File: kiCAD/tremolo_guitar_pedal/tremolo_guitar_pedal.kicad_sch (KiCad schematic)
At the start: 47 parts, among them J1 1/4" Mono Jack, J2 1/4" Mono Jack, J4 Barrel_Jack, J5 UPduino v3.1, SW1 3PDT Footswitch, SW2 3PDT Footswitch, SW3 3PDT Footswitch, SW4 SW_Depth, SW5 SW_Speed, U1 MCP6002-xP, U2 MCP6002-xP, U3 LD1117DT33CTR, U3 MCP6002-xP, U4 NUCLEO-LxxxKx, U5 PCM5102, U7 UPduino_v3.1

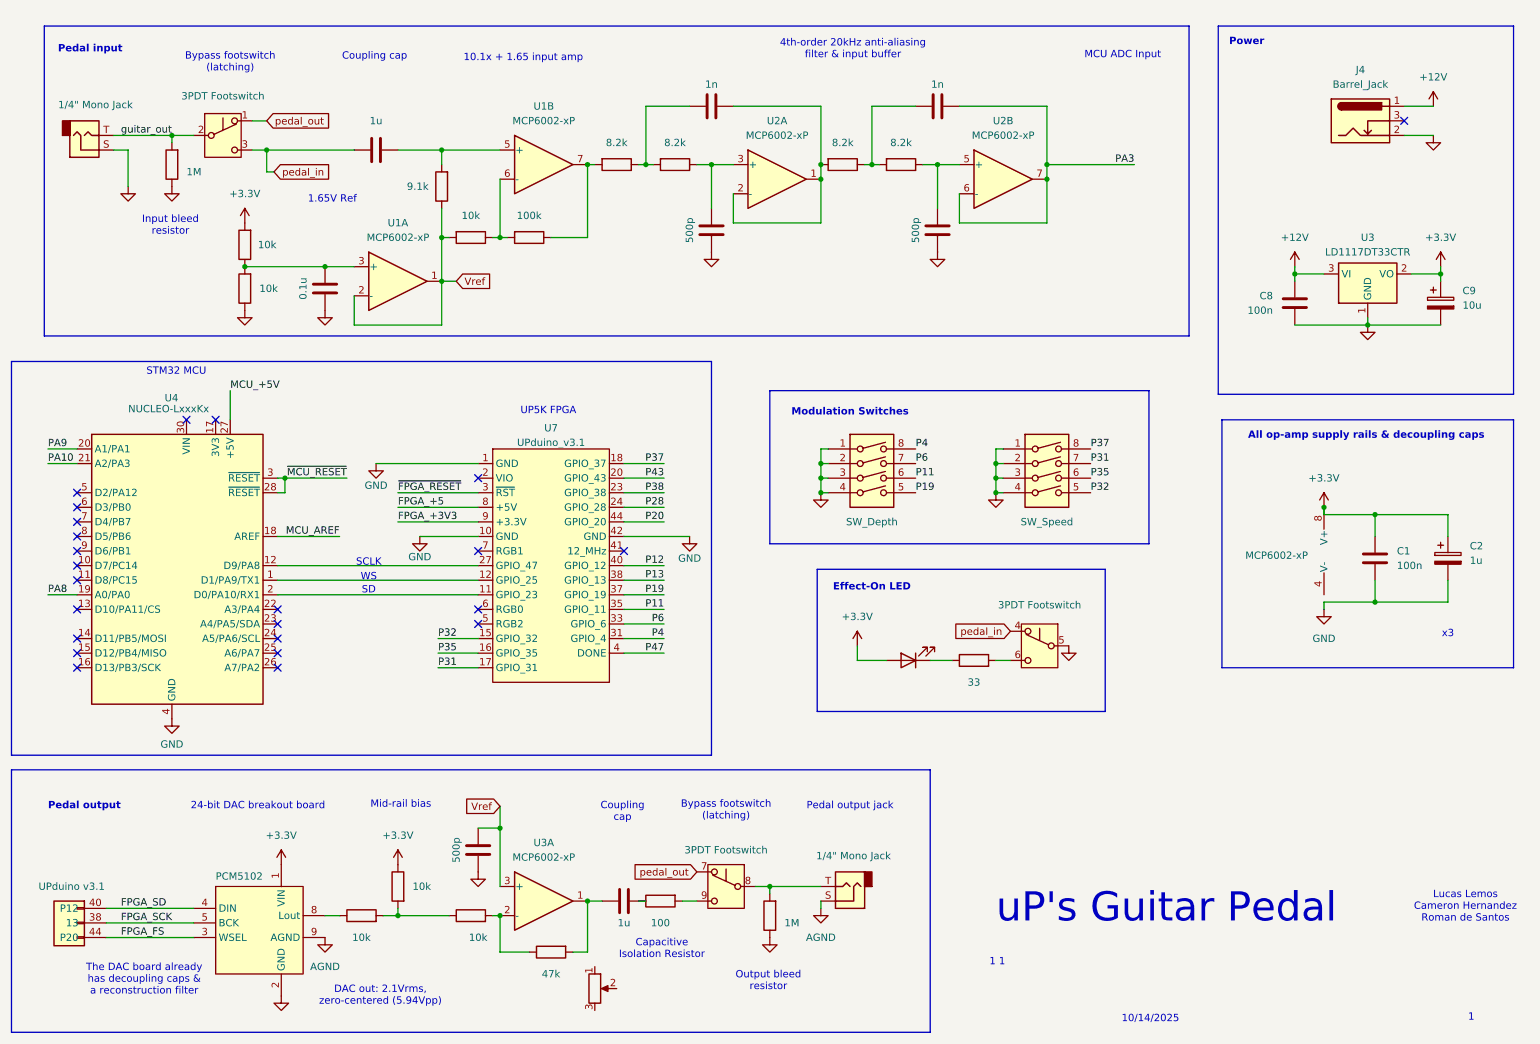
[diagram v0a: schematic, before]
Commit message: Fixed schematic ports
for MCU & FPGA
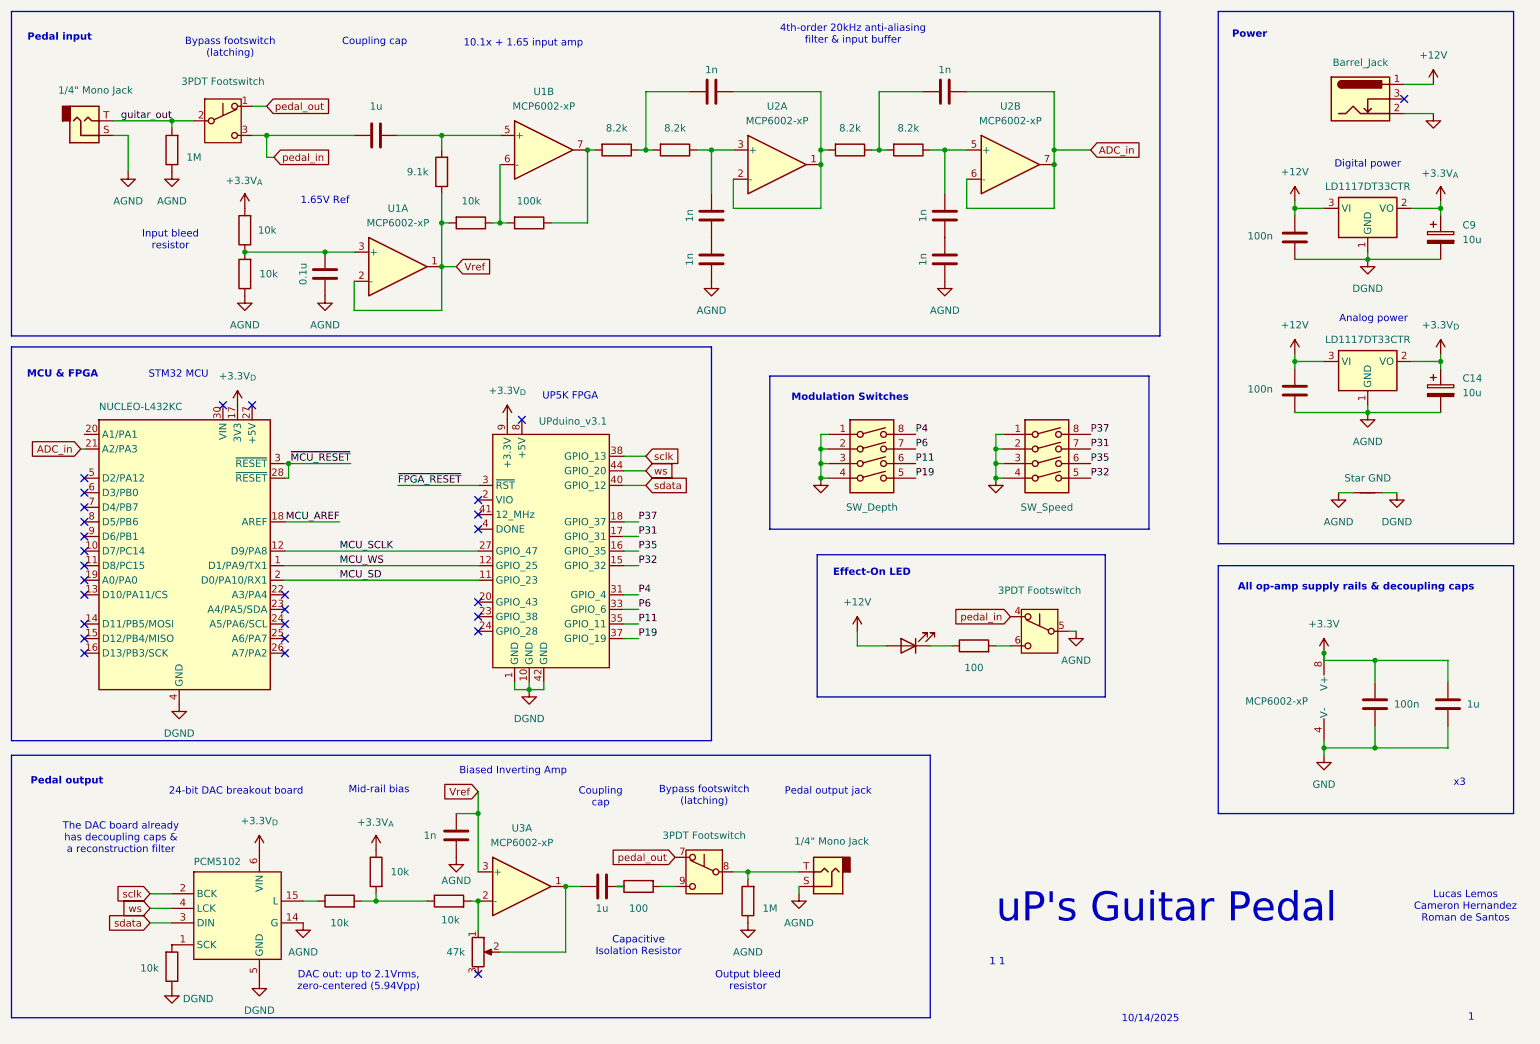
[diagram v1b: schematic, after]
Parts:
- removed C2: 1u, symbol Device:C_Polarized
- removed J5: UPduino v3.1, symbol Connector_Generic:Conn_01x03
- added C14: 10u, symbol Device:C_Polarized
- added C15, C16: 1n, symbol Device:C
- added C2: 1u, symbol Device:C
- added C4: 100n, symbol Device:C
- added NT1: Star GND, symbol Device:NetTie_2
- added U6: LD1117DT33CTR, Package_TO_SOT_THT:TO-220-3_Vertical, symbol Regulator_Linear:LD1117V33
- C10, C11, C12: value 500p -> 1n
- R17: value 47k -> 10k
- R5: value 33 -> 100
- U4: value NUCLEO-LxxxKx -> NUCLEO-L432KC
- speed1: value 10k, log -> 47k
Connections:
- net FPGA_+3V3 is gone; now on net +3.3V_{D}: U7.9 (+3.3V)
- net FPGA_SCK is gone; now on net DGND: U5.5 (GND)
- net P12 is gone; now on net sdata: U7.40 (GPIO_12)
- net P20 is gone; now on net ws: U7.44 (GPIO_20)
- net PA3 is gone; now on net ADC_in: C6.2, U2.6 (-), U2.7
- net +12V: now also D3.2 (A), C4.1, U6.3 (VI)
- net +3.3V: now also C2.1; no longer C9.1, D3.2 (A), R2.2, R9.1, U3.2 (VO), U5.1 (VIN)
- net AGND: now also C10.1, C12.1, C5.1, J1.S, R14.1, R3.1, R6.1, SW2.5 (5B), U5.14 (G), C14.2, C16.1, C4.2, NT1.1, U6.1 (GND); no longer U5.9 (AGND)
- net DGND: now also C8.2, C9.2, R17.1, U3.1 (GND), U4.29 (GND), U4.4 (GND), U7.1 (GND), U7.10 (GND), U7.42 (GND), NT1.2; no longer U5.2 (GND)
- net GND: now also U1.4 (V-), C2.2; no longer C10.1, C11.1, C12.1, C5.1, C8.2, C9.2, J1.S, R14.1, R3.1, R6.1, SW2.5 (5B), U3.1 (GND), U4.29 (GND), U4.4 (GND), U7.1 (GND), U7.10 (GND), U7.42 (GND)
- net at R15.1, U2.5 (+): now also C15.2; no longer C10.2
- net at speed1.1: now also R16.2, U3.2 (-)
- net at speed1.2: now also C13.1, U3.1
- net MCU_WS: now reaches U4.1 (D1/PA9/TX1), U7.12 (GPIO_25)
- net MCU_SCLK: now reaches U4.12 (D9/PA8), U7.27 (GPIO_47)
- net +3.3V_{D}: now reaches U4.17 (3V3)
- net +3.3V_{D}: now also U5.6 (VIN), C14.1, U6.2 (VO)
- net MCU_SD: now reaches U4.2 (D0/PA10/RX1), U7.11 (GPIO_23)
- net at R10.1: now also U5.15 (L); no longer U5.8 (Lout)
- net FPGA_+5: no longer names the net of U7.8 (+5V)
- net FPGA_FS renamed sdata
- net FPGA_SD renamed ws
- net MCU_+5V: no longer names the net of U4.27 (+5V)
- net P13 renamed sclk
- net sclk: now also U5.2 (BCK)
- net P28: no longer names the net of U7.24 (GPIO_28)
- net P38: no longer names the net of U7.23 (GPIO_38)
- net P43: no longer names the net of U7.20 (GPIO_43)
- net P47: no longer names the net of U7.4 (DONE)
- net PA10 renamed ADC_in
- net PA8: no longer names the net of U4.19 (A0/PA0)
- net PA9: no longer names the net of U4.20 (A1/PA1)
- new net: R17.2, U5.1 (SCK)
- new net: C10.2, C11.1
- new net: C15.1, C16.2
- new net +3.3V_{A}: C9.1, R2.2, R9.1, U3.2 (VO)
- no-connect marks 24 -> 28
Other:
- note added: "Analog power"
- note added: "Biased Inverting Amp"
- note added: "DAC out: up to 2.1Vrms, zero-centered (5.94Vpp)"
- note added: "Digital power"
- note added: "MCU & FPGA"
- note removed: "DAC out: 2.1Vrms, zero-centered (5.94Vpp)"
- note removed: "MCU ADC Input"
- note removed: "SCLK"
- note removed: "SD"
- note removed: "WS"
- moved on the sheet: C9, U1A, U1B, U2A, U2B, U3A
